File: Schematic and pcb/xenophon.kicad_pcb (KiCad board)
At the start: 2 copper layers, 301.4 x 138.2 mm, 189 parts, among them J1 USB_C_Receptacle, J2 AudioJack3, J3 AudioJack3, SW1 SW_Push, SW10 SW_Push, SW11 SW_Push, SW12 SW_Push, SW13 SW_Push, SW14 SW_Push, SW15 SW_Push, SW16 SW_Push, SW17 SW_Push, SW18 SW_Push, SW19 SW_Push, SW2 SW_Push, SW20 SW_Push, SW21 SW_Push, SW22 SW_Push, SW23 SW_Push, SW24 SW_Push, SW25 SW_Push, SW26 SW_Push, SW27 SW_Push, SW28 SW_Push, SW29 SW_Push, SW3 SW_Push, SW30 SW_Push, SW31 SW_Push, SW32 SW_Push, SW33 SW_Push, SW34 SW_Push, SW35 SW_Push, SW38 SW_Push, SW39 SW_Push, SW4 SW_Push, SW40 SW_Push, SW41 SW_Push, SW42 SW_Push, SW43 SW_Push, SW44 SW_Push, SW45 SW_Push, SW46 SW_Push, SW47 SW_Push, SW48 SW_Push, SW49 SW_Push, SW5 SW_Push, SW50 SW_Push, SW51 SW_Push, SW52 SW_Push, SW53 SW_Push, SW54 SW_Push, SW55 SW_Push, SW56 SW_Push, SW57 SW_Push, SW58 SW_Push, SW59 SW_Push, SW6 SW_Push, SW60 SW_Push, SW61 SW_Push, SW62 SW_Push, SW63 SW_Push, SW64 SW_Push, SW65 SW_Push, SW66 SW_Push, SW67 SW_Push, SW68 SW_Push, SW69 SW_Push, SW7 SW_Push, SW70 SW_Push, SW71 SW_Push, SW72 SW_Push, SW8 SW_Push, SW9 SW_Push, U1 ATmega32U4-AU, U2 ATmega32U4-AU, Y1 Crystal, Y2 Crystal

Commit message: Changed name
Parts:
- renumbered TP8 to D+, TP5 to D+, TP7 to D-, TP6 to D-, TP1 to GND, TP3 to GND, TP2 to RESET, TP4 to RESET
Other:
- board text added: "Xenophon"
- board text removed: "Fasth T1"

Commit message: Wrote the intro readme.
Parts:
- TP1, TP3: renamed from GND; footprint TestPoint:TestPoint_THTPad_1.0x1.0mm_Drill0.5mm -> TestPoint:TestPoint_THTPad_2.0x2.0mm_Drill1.0mm
- TP2, TP4: renamed from RESET; footprint TestPoint:TestPoint_THTPad_1.0x1.0mm_Drill0.5mm -> TestPoint:TestPoint_THTPad_2.0x2.0mm_Drill1.0mm
- TP5, TP8: renamed from D+; footprint TestPoint:TestPoint_THTPad_1.0x1.0mm_Drill0.5mm -> TestPoint:TestPoint_THTPad_2.0x2.0mm_Drill1.0mm
- TP6, TP7: renamed from D-; footprint TestPoint:TestPoint_THTPad_1.0x1.0mm_Drill0.5mm -> TestPoint:TestPoint_THTPad_2.0x2.0mm_Drill1.0mm
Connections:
- Y1 pad 2: GND -> Net-(C6-Pad1)
- Y1 pad 3: Net-(C6-Pad1) -> (no net)
- Y1 pad 4: GND -> (no net)
- Y2 pad 2: Net-(C10-Pad2) -> Net-(C9-Pad1)
- Y2 pad 3: Net-(C9-Pad1) -> (no net)
- Y2 pad 4: Net-(C10-Pad2) -> (no net)

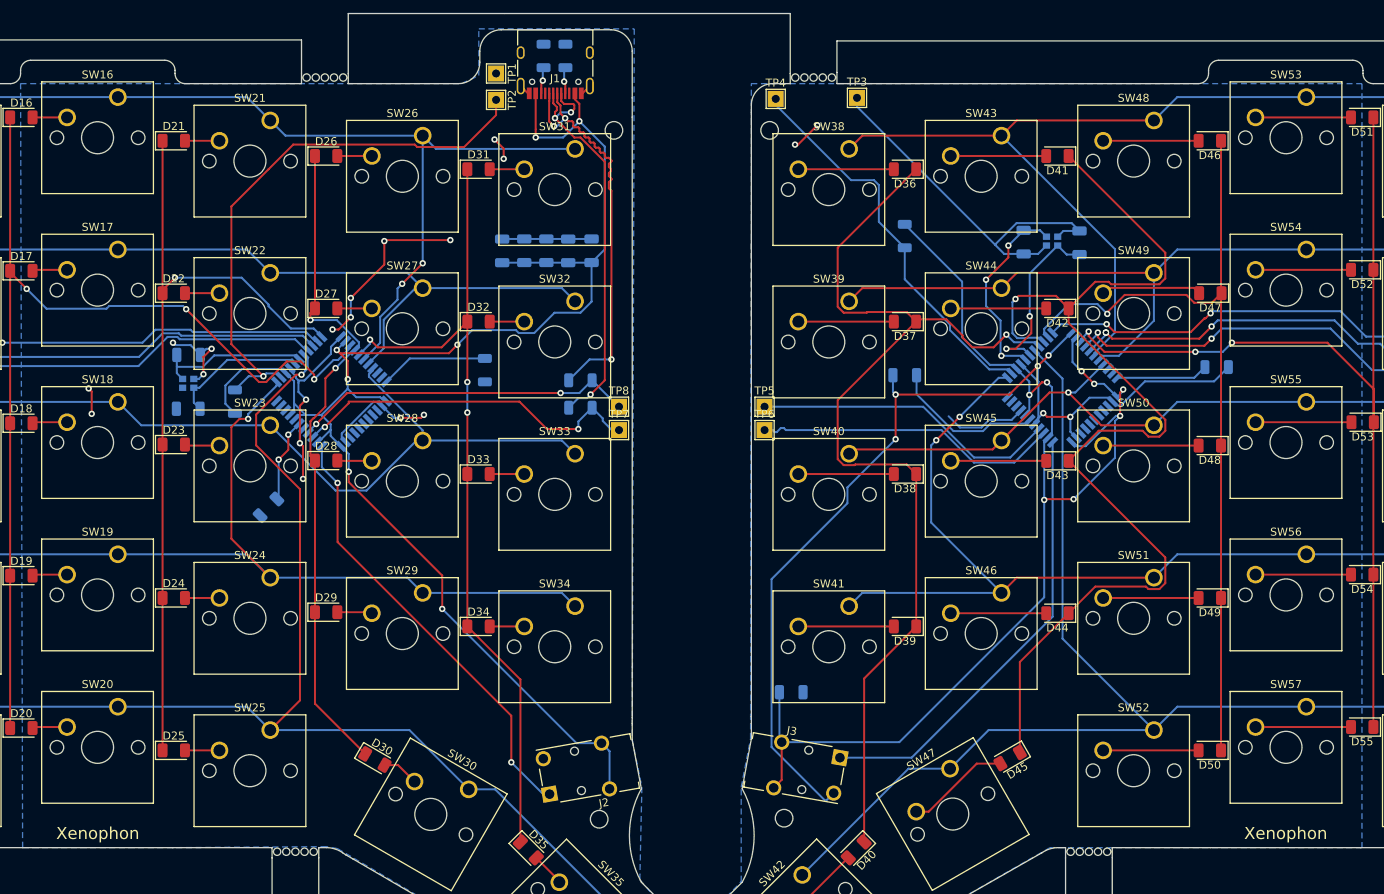
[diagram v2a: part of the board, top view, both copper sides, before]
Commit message: Added images and title block for the schematic.
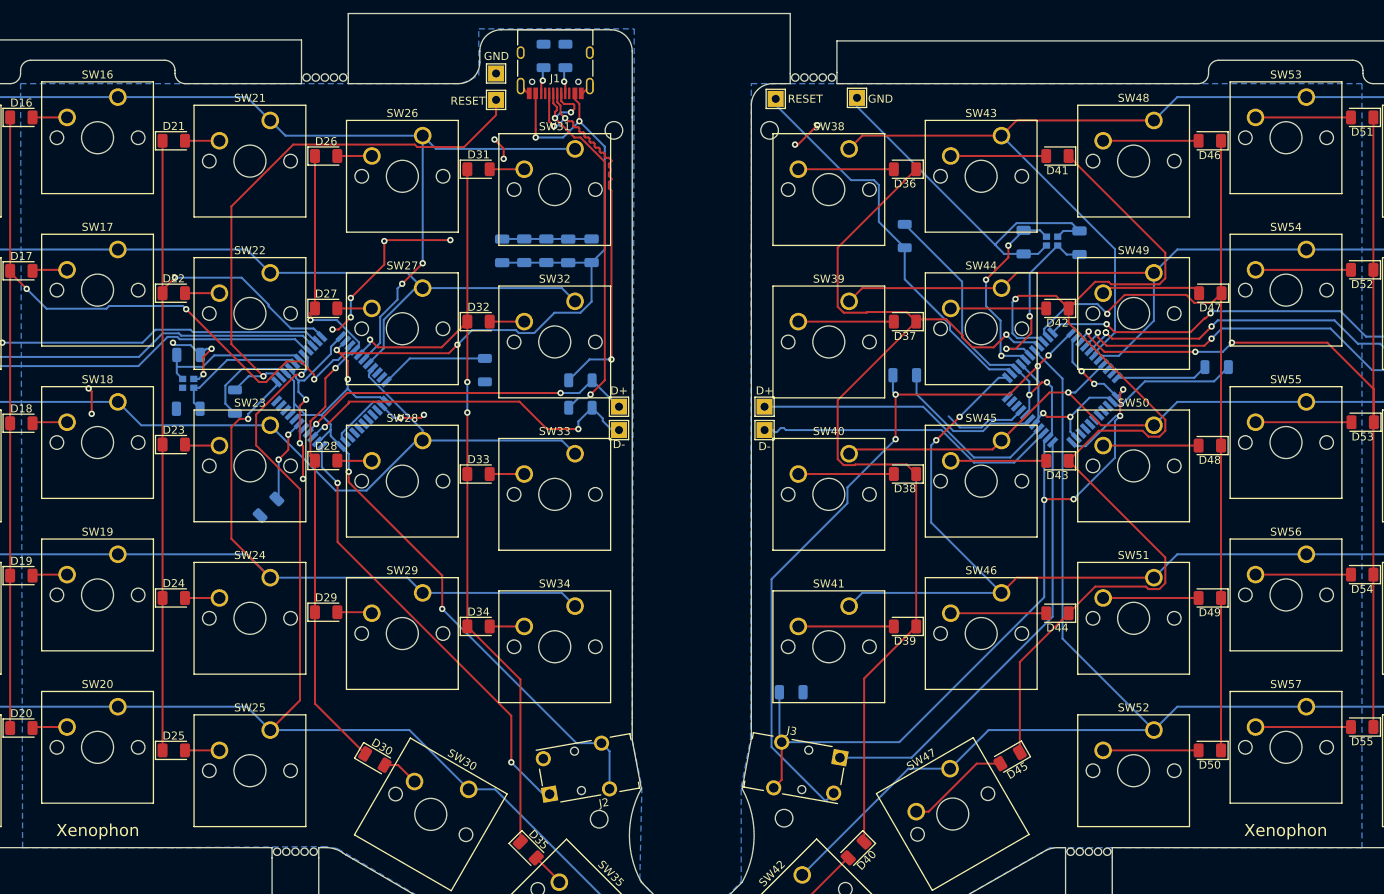
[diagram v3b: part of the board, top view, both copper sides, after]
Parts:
- renumbered TP8 to D+, TP5 to D+, TP7 to D-, TP6 to D-, TP3 to GND, TP1 to GND, TP4 to RESET, TP2 to RESET

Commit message: Updated pcb and projekt files.
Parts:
- J1: footprint Connector_USB:USB_C_Receptacle_HRO_TYPE-C-31-M-12 -> XenophonFootprintLibrary:USB_C_Receptacle_HRO_TYPE-C-31-M-12
- J2, J3: footprint Connector_Audio:Jack_3.5mm_Switronic_ST-005-G_horizontal -> XenophonFootprintLibrary:Jack_3.5mm_Switronic_ST-005-G_horizontal
- SW1, SW2, SW3, SW4, SW5, SW68, SW69, SW70, SW71, SW72: footprint keyswitch:SW_Cherry_MX_1.50u_PCB -> XenophonFootprintLibrary:SW_Cherry_MX_1.50u_PCB
- SW10, SW11, SW12, SW13, SW14, SW15, SW16, SW17, SW18, SW19, SW20, SW21, SW22, SW23, SW24, SW25, SW26, SW27, SW28, SW29, SW30, SW31, SW32, SW33, SW34, SW35, SW38, SW39, SW40, SW41, SW42, SW43, SW44, SW45, SW46, SW47, SW48, SW49, SW50, SW51, SW52, SW53, SW54, SW55, SW56, SW57, SW58, SW59, SW6, SW60, SW61, SW62, SW63, SW64, SW65, SW66, SW67, SW7, SW8, SW9: footprint keyswitch:SW_Cherry_MX_1.00u_PCB -> XenophonFootprintLibrary:SW_Cherry_MX_1.00u_PCB
- renumbered RESET to Reset
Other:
- net class Default removed
- board text added: "@lillkakan"
- board text removed: "@JesperFasth"

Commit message: Updated PCB files to the new verison of kicad.
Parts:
- removed the REF** at (2.65, 132.5)
- removed the REF** at (138.3, 128.9)
- removed the REF** at (2.65, 43.6)
- removed the REF** at (134.3, 151.1)
- removed the REF** at (297.1, 43.6)
- removed the REF** at (161.4, 128.8)
- removed the REF** at (297.1, 132.5)
- removed the REF** at (159.6, 42.8)
- removed the REF** at (140.2, 42.8)
- added REF**: MountingHole_2.7mm_M2.5_ISO7380, MountingHole:MountingHole_2.7mm_M2.5_ISO7380, F.Cu at (2.08, 133.1)
- added REF**: MountingHole_2.7mm_M2.5_ISO7380, MountingHole:MountingHole_2.7mm_M2.5_ISO7380, F.Cu at (139.2, 129.4)
- added REF**: MountingHole_2.7mm_M2.5_ISO7380, MountingHole:MountingHole_2.7mm_M2.5_ISO7380, F.Cu at (134.2, 150.7)
- added REF**: MountingHole_2.7mm_M2.5_ISO7380, MountingHole:MountingHole_2.7mm_M2.5_ISO7380, F.Cu at (160.7, 129.3)
- added REF**: MountingHole_2.7mm_M2.5_ISO7380, MountingHole:MountingHole_2.7mm_M2.5_ISO7380, F.Cu at (297.7, 133.1)
- added REF**: MountingHole_2.7mm_M2.5_ISO7380, MountingHole:MountingHole_2.7mm_M2.5_ISO7380, F.Cu at (2.08, 43.4)
- added REF**: MountingHole_2.7mm_M2.5_ISO7380, MountingHole:MountingHole_2.7mm_M2.5_ISO7380, F.Cu at (297.7, 43.4)
- added REF**: MountingHole_2.7mm_M2.5_ISO7380, MountingHole:MountingHole_2.7mm_M2.5_ISO7380, F.Cu at (160.2, 41.0)
- added REF**: MountingHole_2.7mm_M2.5_ISO7380, MountingHole:MountingHole_2.7mm_M2.5_ISO7380, F.Cu at (139.5, 40.8)
- REF**: value MountingHole_2.2mm_M2_ISO7380 -> MountingHole_2.7mm_M2.5_ISO7380; footprint MountingHole:MountingHole_2.2mm_M2_ISO7380 -> MountingHole:MountingHole_3.2mm_M3_ISO7380
- moved Reset 3.77 mm to (164.2, 38.8)
- moved GND 1.36 mm to (171.9, 38.7)
- moved REF** 0.28 mm to (165.5, 150.8)
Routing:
- net Net-(R5-Pad1): track 49.6 -> 47.2 mm
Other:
- board size 301.4 x 138.2 mm -> 301.4 x 124.2 mm
